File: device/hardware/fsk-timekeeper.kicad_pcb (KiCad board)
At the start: 2 copper layers, 92 x 57 mm, 27 parts, among them J1 SENSOR, SW1 SW_SPST, U1 SuperMini nRF52840, U2 Ai-Thinker Ra-01SH, U3 TPS61040DBV, U4 ATGM336H

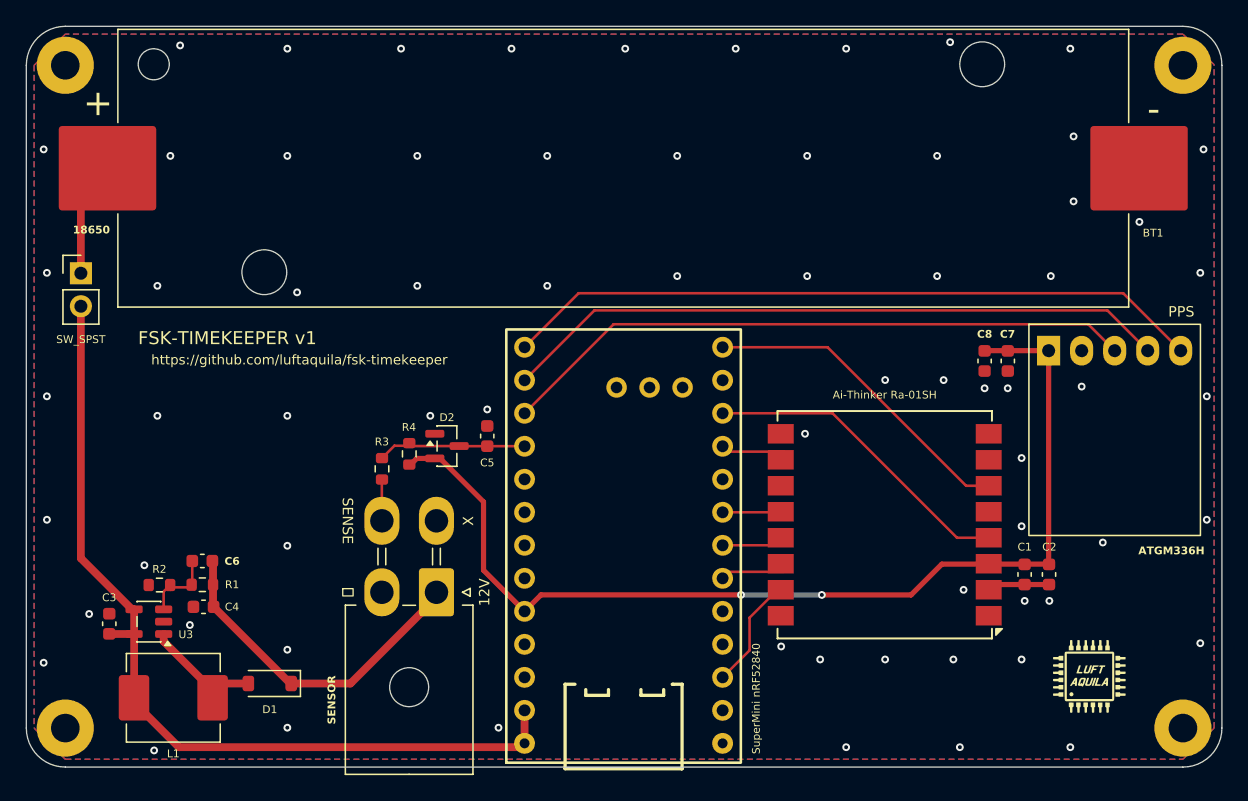
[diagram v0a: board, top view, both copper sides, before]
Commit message: fix: remove the track pieces that lie inside pads
Drop 39 short segments that sit entirely inside pads, including the two
stubs on the unconnected U1 pads 17 and 19. Vias and footprints are
unchanged and the zones are refilled.

Co-Authored-By: Claude Opus 5.5 <noreply@anthropic.com>
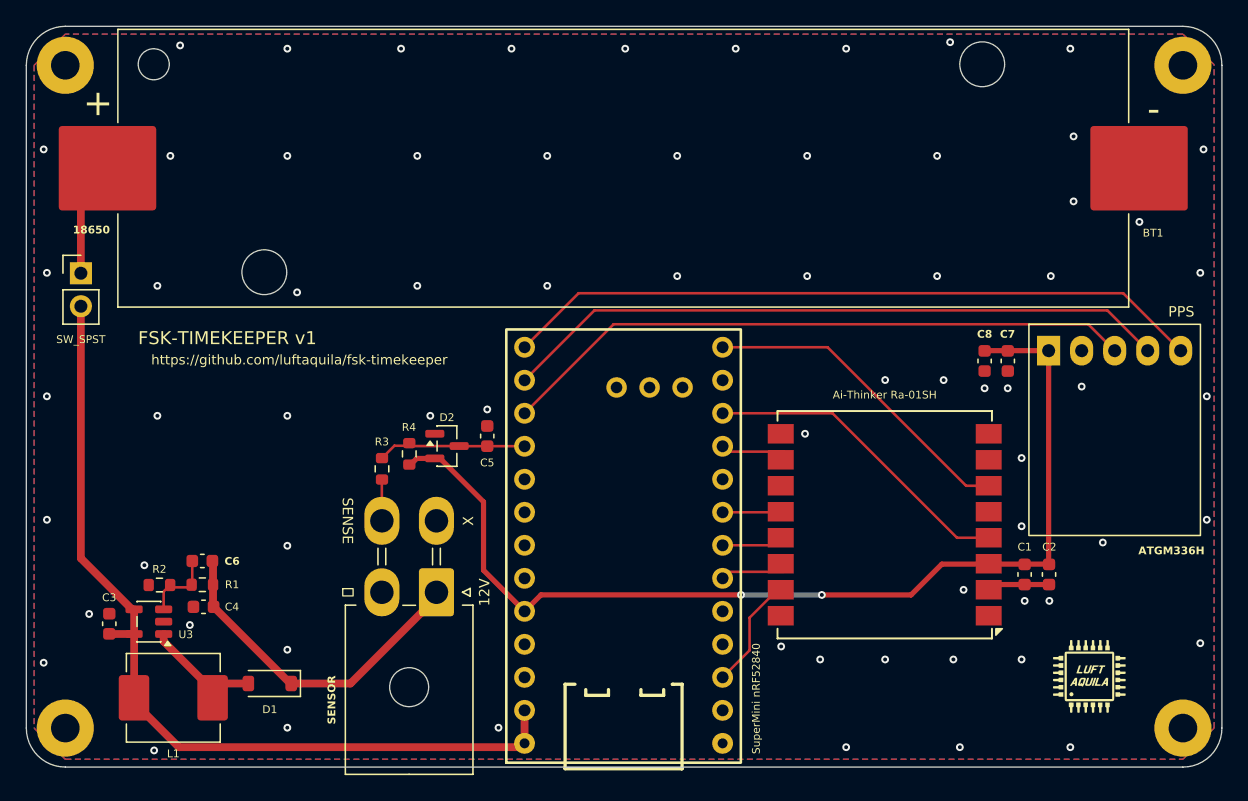
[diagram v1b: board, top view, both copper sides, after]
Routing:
- net Net-(BT1-+): track 8.93 -> 6.03 mm
- net /BUSY: track 6.65 -> 4.33 mm
- net /MOSI: track 5.98 -> 4.25 mm
- net /MISO: track 6.43 -> 4.79 mm
- net +BATT: track 68.3 -> 67.4 mm
- net +3.3V: track 80.5 -> 79.7 mm
- net +12V: track 26.4 -> 25.7 mm
- net /NSS: track 9.11 -> 8.49 mm
- net Net-(U3-FB): track 5.73 -> 5.13 mm
- net Net-(D1-A): track 8.12 -> 7.55 mm
